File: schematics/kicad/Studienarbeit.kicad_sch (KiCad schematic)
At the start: 44 parts

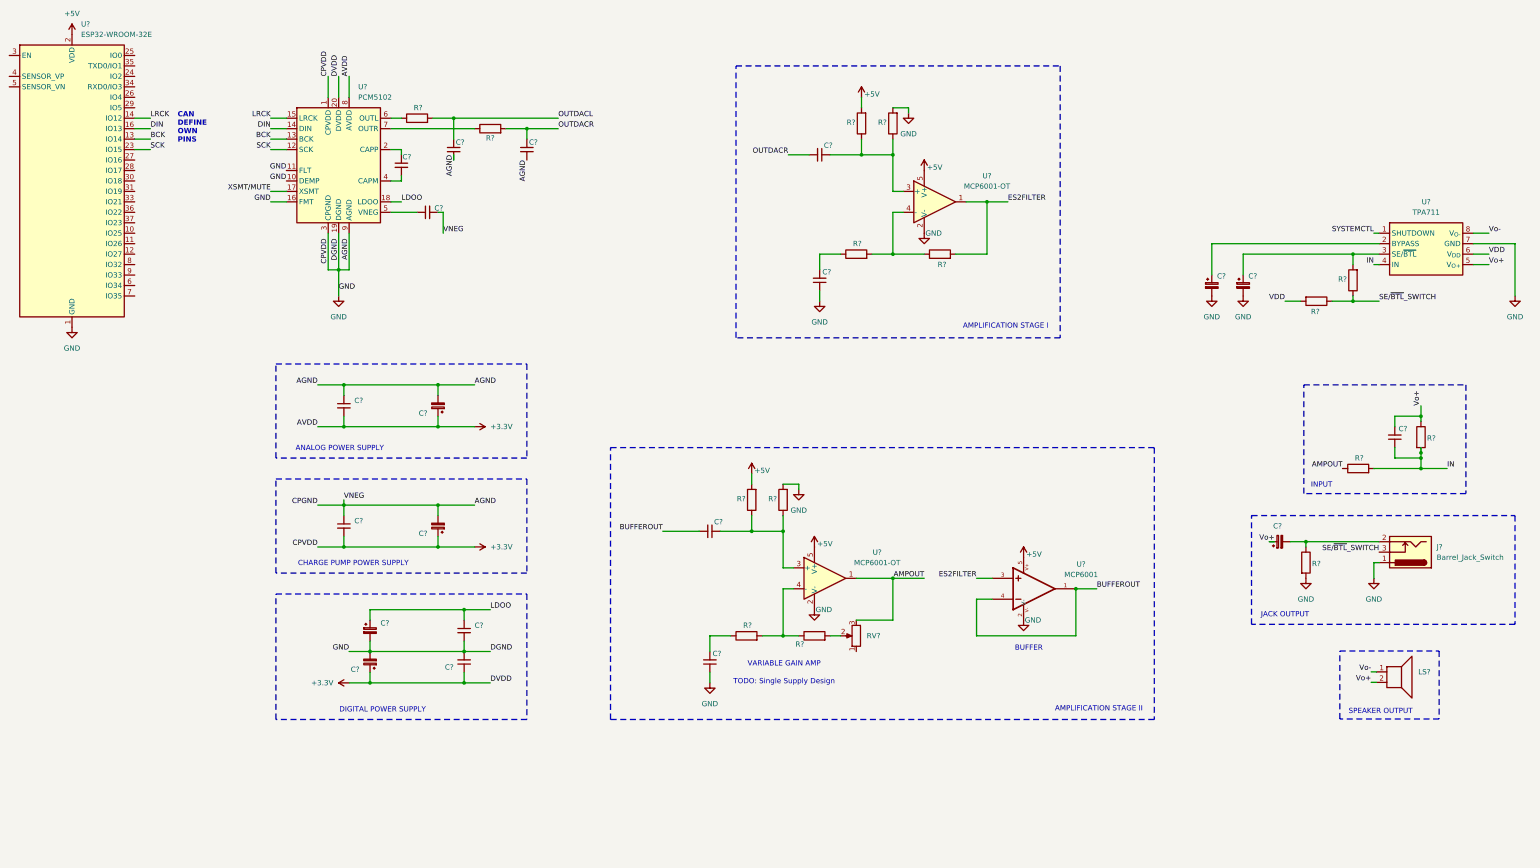
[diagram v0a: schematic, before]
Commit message: KiCad: rewired PCM5120 I/O pins and dimentioned Rs and Cs
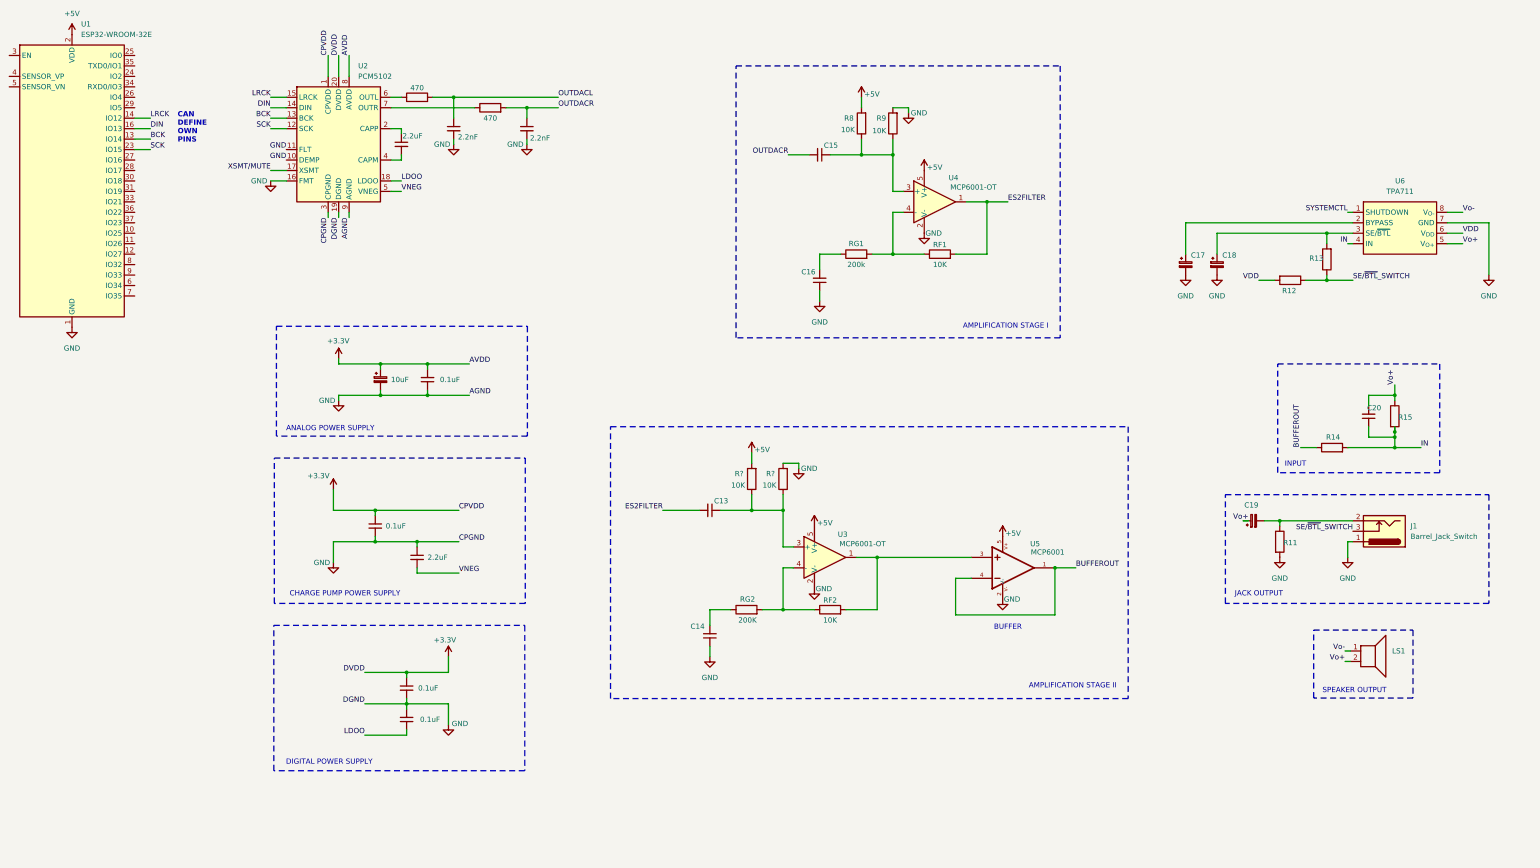
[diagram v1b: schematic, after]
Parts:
- removed C? (x2): C_Small, symbol Device:C_Small
- removed C? (x3): C_Polarized_Small, symbol Device:C_Polarized_Small
- removed R? (x3): R, symbol Device:R
- removed RV?: R_Potentiometer, symbol Device:R_Potentiometer
- added 0.1uF, 2.2uF: C_Small, symbol Device:C_Small
- added R? (x2): 10K, LED_SMD:LED_0805_2012Metric_Pad1.15x1.40mm_HandSolder, symbol Device:R
- added RF2: 10K, Resistor_SMD:R_0805_2012Metric_Pad1.20x1.40mm_HandSolder, symbol Device:R
- C16: renamed from C?; value C_Small -> 10uF
- R1, R2: renamed from R?; value R -> 470; footprint (none) -> Resistor_SMD:R_0805_2012Metric_Pad1.20x1.40mm_HandSolder
- R8: renamed from R?; value R -> 10K; footprint (none) -> LED_SMD:LED_0805_2012Metric_Pad1.15x1.40mm_HandSolder
- R9, RF1: renamed from R?; value R -> 10K; footprint (none) -> Resistor_SMD:R_0805_2012Metric_Pad1.20x1.40mm_HandSolder
- RG1: renamed from R?; value R -> 200k; footprint (none) -> LED_SMD:LED_0805_2012Metric_Pad1.15x1.40mm_HandSolder
- RG2: renamed from R?; value R -> 200K; footprint (none) -> Resistor_SMD:R_0805_2012Metric_Pad1.20x1.40mm_HandSolder
- gave numbers to parts that had none: 24
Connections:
- net +3.3V: now also 0.1uF.1; no longer 0.1uF.1, 0.1uF.2, 0.1uF.2, 10uF.2, 2.2nF.2, 2.2nF.2, C14.1, C16.1, C17.2, C18.2, J1.1, R11.2, R9.2, U1.1 (GND), U1.15 (GND), U1.38 (GND), U1.39 (GND), U2.10 (DEMP), U2.11 (FLT), U2.16 (FMT), U2.19 (DGND), U2.3 (CPGND), U2.9 (AGND), U3.2 (V-), U4.2 (V-), U5.2 (V-), U6.7 (GND)
- net +5V: now also R?.2
- net BUFFEROUT: now also R14.1; no longer C13.2
- net ES2FILTER: now also C13.2; no longer U5.3
- net at C13.1, U3.3 (+): now also R?.1, R?.1
- net VNEG: now reaches U2.5 (VNEG)
- net VNEG: now also 2.2uF.2
- net at RG2.2, U3.4 (-): now also RF2.1
- net AMPOUT: no longer names the net of U3.1
- net AMPOUT: now also U5.3, RF2.2; no longer R14.1
- new net GND: 0.1uF.1, 0.1uF.2, 0.1uF.2, 0.1uF.2, 10uF.2, 2.2nF.2, 2.2nF.2, 2.2uF.1, C14.1, C16.1, C17.2, C18.2, J1.1, R11.2, R9.2, R?.2, U1.1 (GND), U1.15 (GND), U1.38 (GND), U1.39 (GND), U2.10 (DEMP), U2.11 (FLT), U2.16 (FMT), U2.19 (DGND), U2.3 (CPGND), U2.9 (AGND), U3.2 (V-), U4.2 (V-), U5.2 (V-), U6.7 (GND)
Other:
- note removed: "TODO: Single Supply Design"
- note removed: "VARIABLE GAIN AMP"
- moved on the sheet: 0.1uF, 10uF, 2.2nF, 2.2uF, C13, C14, C17, C18, C19, C20, J1, LS1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

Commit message: KiCad: Rewired the TPA711 I/Os and dimentioned Rs and Cs
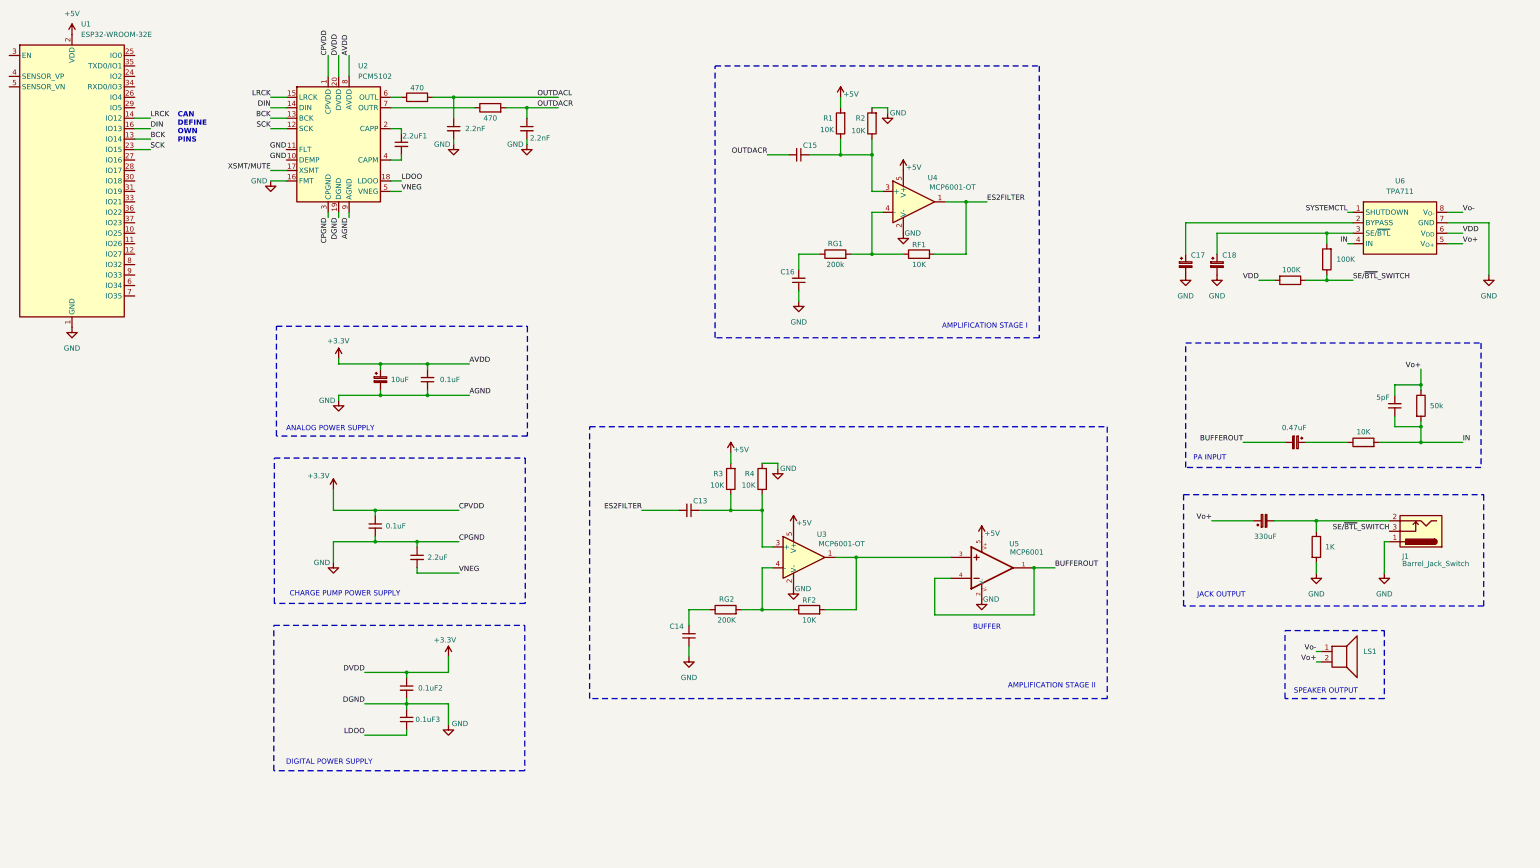
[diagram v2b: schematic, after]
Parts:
- added CI_TPA711: 0.47uF, symbol Device:C_Polarized_Small
- CC_TPA711: renamed from C19; value C_Polarized_Small -> 330uF
- CF_TPA711: renamed from C20; value C_Small -> 5pF
- R11: value R -> 1K; footprint (none) -> Resistor_SMD:R_0805_2012Metric_Pad1.20x1.40mm_HandSolder
- R12, R13: value R -> 100K; footprint (none) -> Resistor_SMD:R_0805_2012Metric_Pad1.20x1.40mm_HandSolder
- RF_TPA711: renamed from R15; value R -> 50k; footprint (none) -> Resistor_SMD:R_0805_2012Metric_Pad1.20x1.40mm_HandSolder
- RI_TPA711: renamed from R14; value R -> 10K; footprint (none) -> Resistor_SMD:R_0805_2012Metric_Pad1.20x1.40mm_HandSolder
- gave numbers to parts that had none: 2
- renumbered 0.1uF to 0.1uF2, 0.1uF to 0.1uF3, 2.2uF to 2.2uF1, R8 to R1, R9 to R2, R1 to ROUTDACL, R2 to ROUTDACR
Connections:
- net BUFFEROUT: now also CI_TPA711.2; no longer RI_TPA711.1
- new net: CI_TPA711.1, RI_TPA711.1
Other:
- note added: "PA INPUT"
- note removed: "INPUT"
- moved on the sheet: C13, C14, C15, C16, J1, LS1, R1, R2, R3, R4, RF1, RF2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

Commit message: KiCad: Grafics.
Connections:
- no-connect marks 0 -> 23
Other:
- note added: "ESP32-WROOM-32E"
- note added: "PCM5102"
- note added: "TPA711"
- moved on the sheet: 0.1uF, 0.1uF2, 0.1uF3, 10uF, 2.2nF, 2.2uF, 2.2uF1, C13, C14, C15, C16, C17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
